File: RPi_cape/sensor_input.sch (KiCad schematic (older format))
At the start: 39 parts, among them U5 LM2903, U6 LMC7101B, U7 LMC7101B

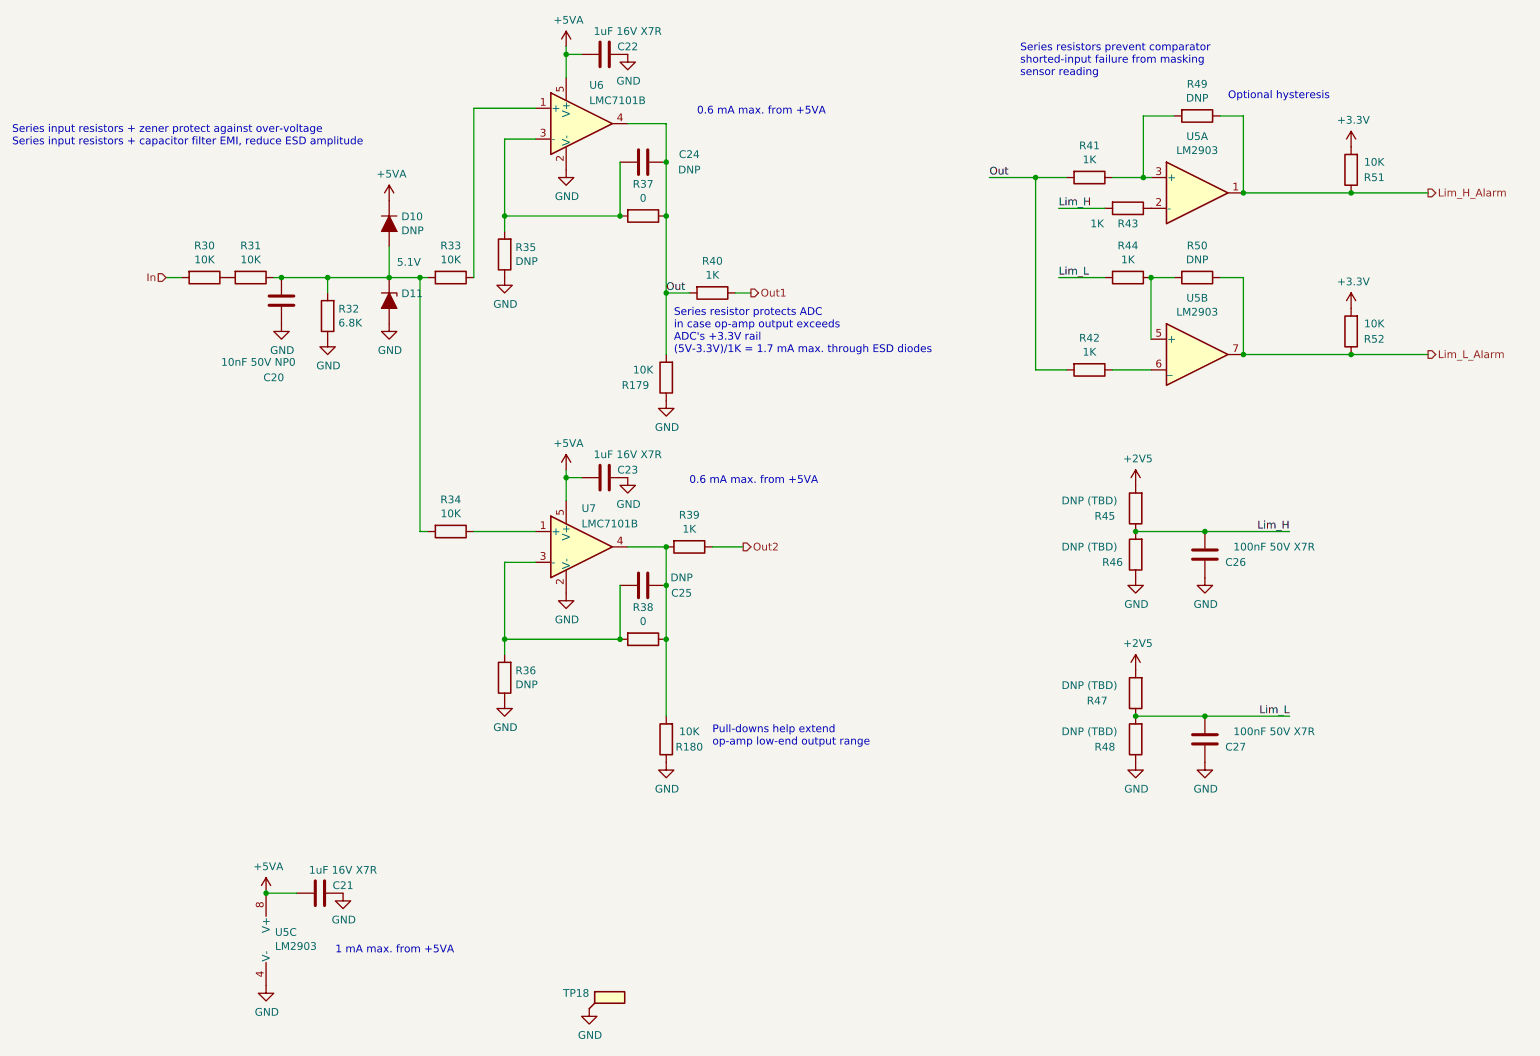
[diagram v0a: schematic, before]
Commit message: Analog upgrades and extra encoder connectors
Renamed a few files
Removed "costing BOM" as difficult to keep up to date, easy to regenerate
Toughened under-voltage detect circuits by adding hysteresis to +5V detect for +BATT diode-OR (R236), filtering to power-down alarm detect input (C85)
Added connector options (J15, J21) for Grayhill C14-series rotary encoder with cable
Changed R190 from 3K to 2.4K to increase overhead on base current required for saturation, and consolidate BOM
Added 3 solderable testpoints for expanding CPLD pin options (TP44-46), adjusted some CPLD pin assignments to allow physical routing to pins
Fixed valve motion detector by changing comparator's hysteresis to AC-only, changing NPN's series resistor to 1K (allows low-enough DC level to count as logic low), and adding optional filtering cap C115 to offset divider
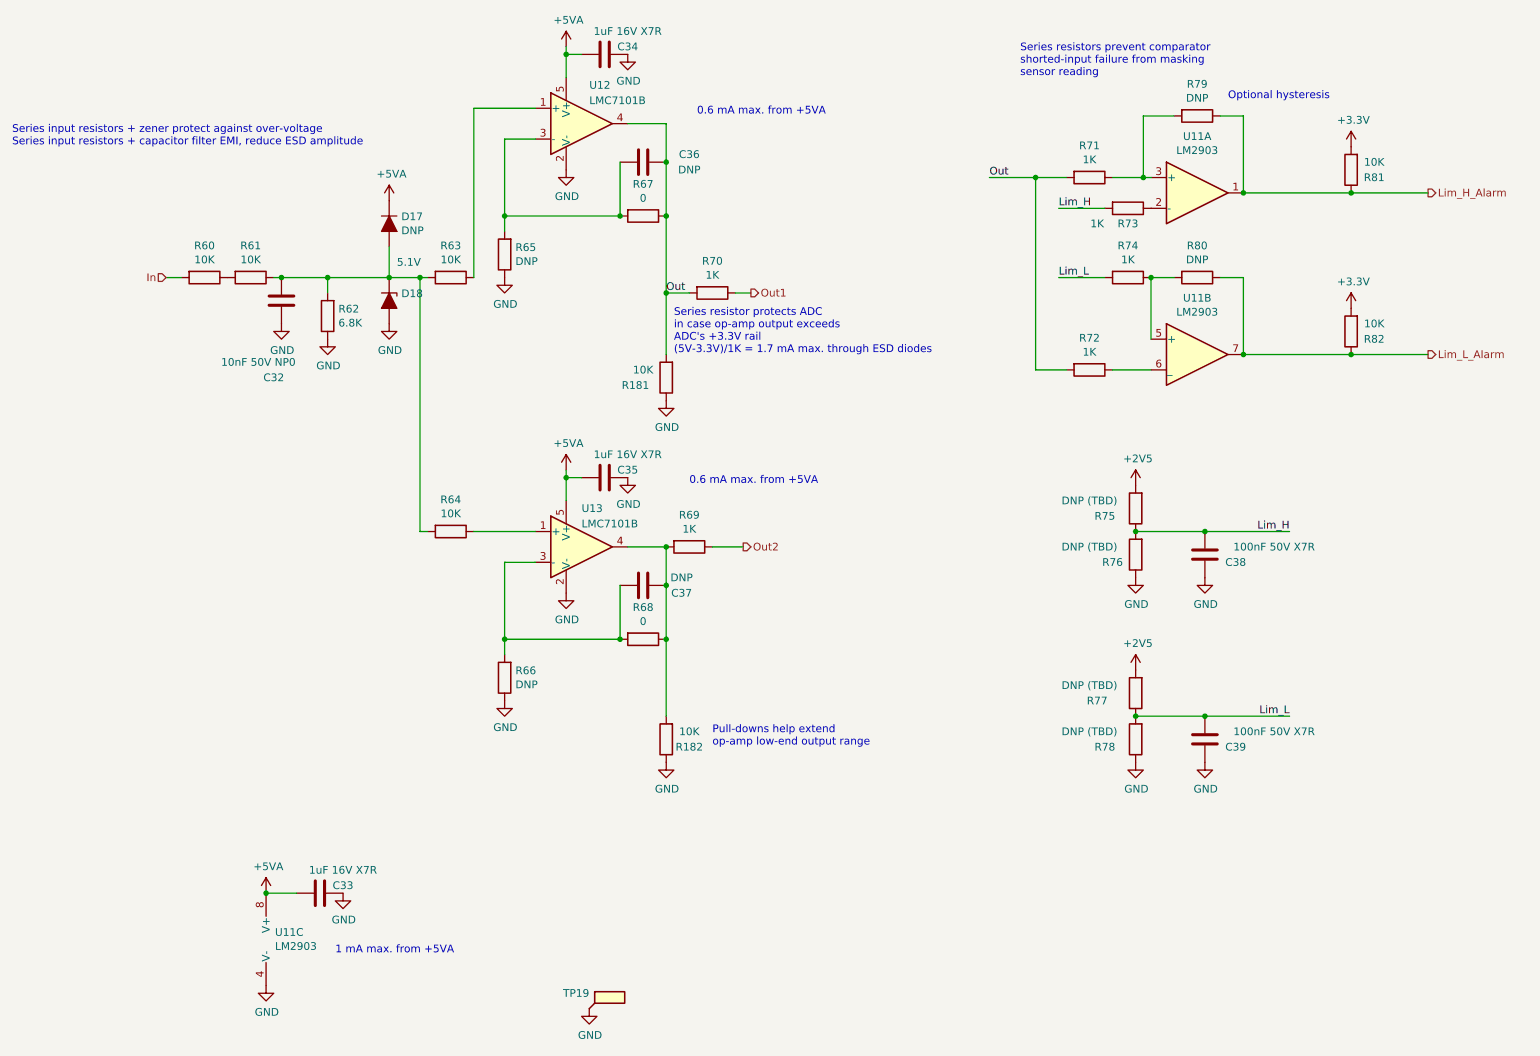
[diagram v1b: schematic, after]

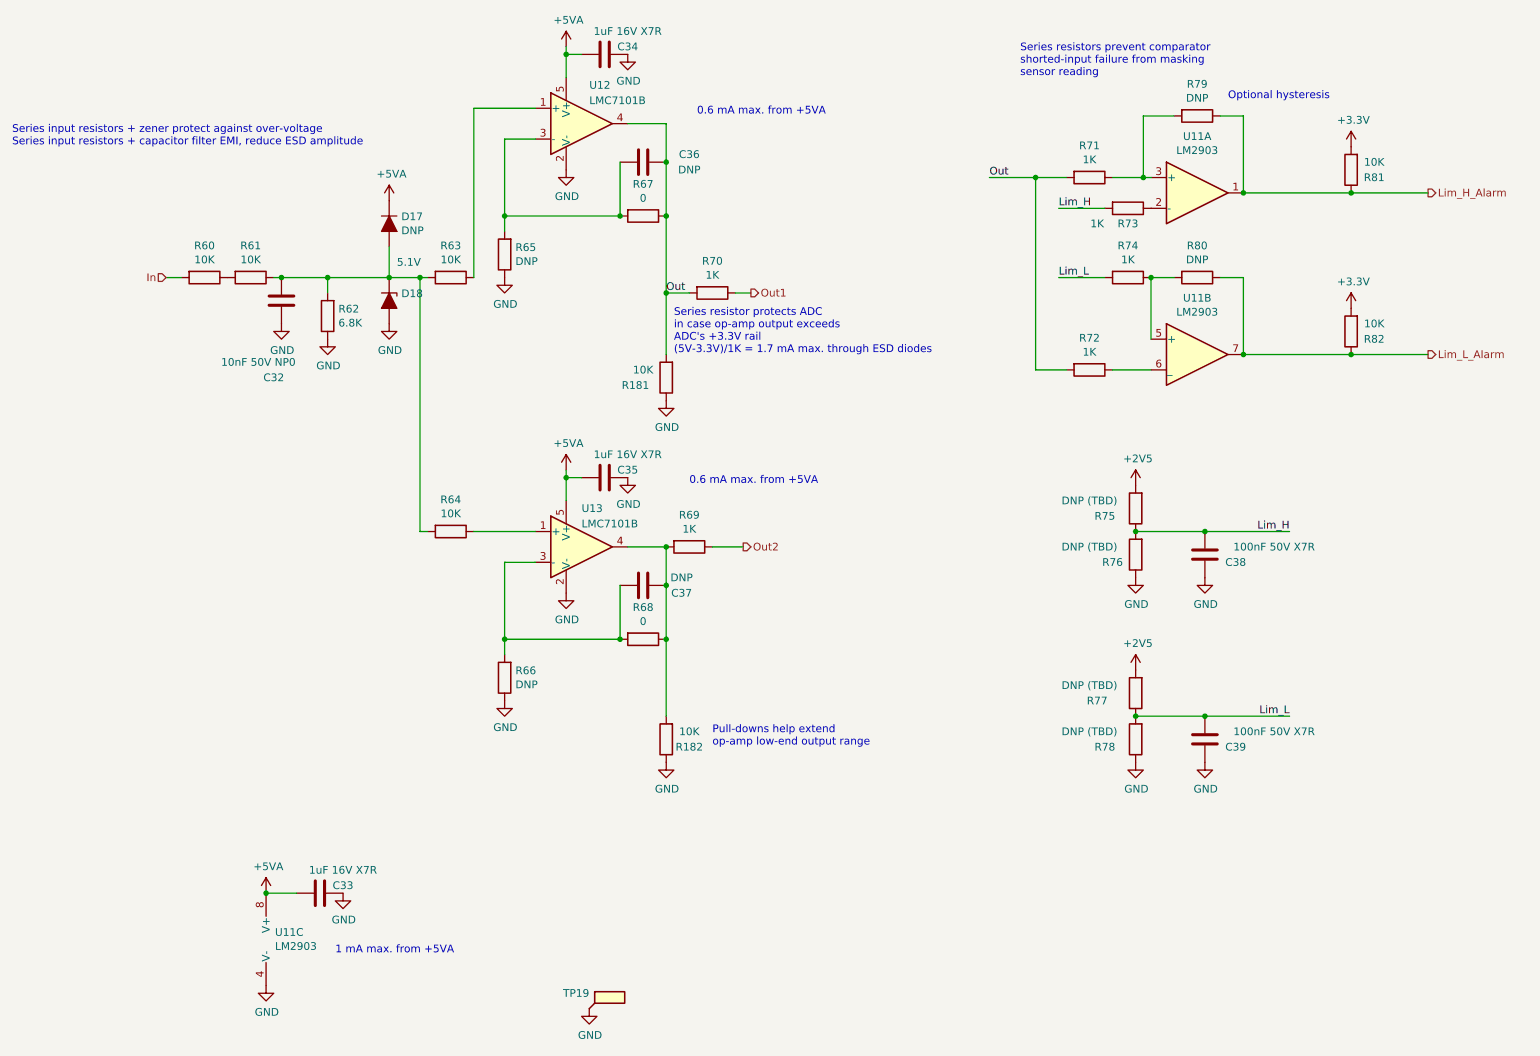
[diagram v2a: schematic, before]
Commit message: Admin (naming, license), improvements based on testing
Updated name on schematic, PCB silkscreen
Added 3 mounting holes on inside area of board for better mechanical robustness
Removed extra unused pressure sensor barb packages from library
Fixed Phoenix spring connector footprints, and added 3D models from Phoenix website
Added 3D models to TE encoder connector footprints, QFP-100 for CPLD, and 5019 testpoint
Changed DIAG_EN pin connection from valve drivers from +24V (too high) to +3.3V
Added CERN licensing terms
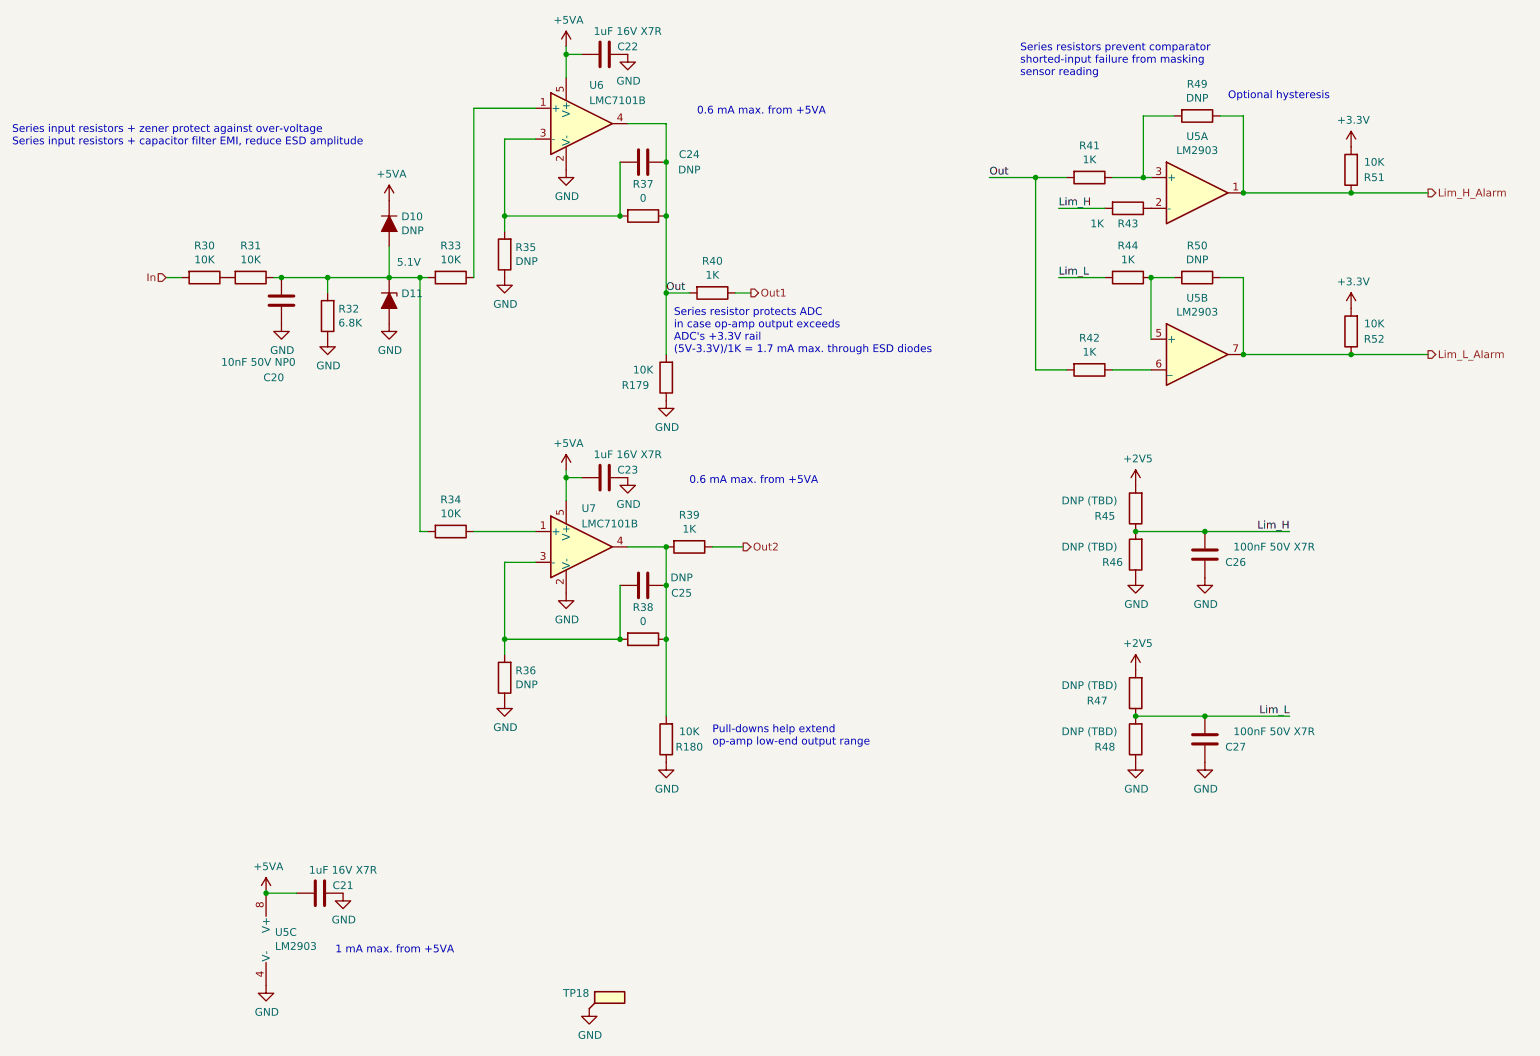
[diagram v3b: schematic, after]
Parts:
- TP18: footprint TestPoint:TestPoint_Keystone_5019_Minature -> Ventilator:TestPoint_Keystone_5019_Minature

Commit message: Design update based on changed software/firmware/pneumatics reqs
Swapped Max V CPLD for Max 10 FPGA
Removed +1.8V regulator and monitoring (in power-down alarm) because Max 10 FPGA has internal regulator
Changed FPGA's valve-enable pull-downs from 1K to 10K because Max 10 floats the outputs during power-up/programming (instead of Max V's internal pull-ups)
Changed low-pressure sensor from BMP388 to MS5607 for more manufacturable footprint / high availability, and moved all digital pressure sensors to daughterboard for repairability
Changed single op-amps in analog pressure sensor inputs / valve motion detect circuits to TLV6001 for better bias current, correct footprint
Removed excessive DNP components in analog pressure sensor inputs to ease routing with new op-amps
Added double-inverted hysteresis circuit to valve motion detect that won't drive U38's '+' input above the rail and cause latchup
Added optional pull-down resistors to valve-motiion-detect op-amps to allow output voltages to swing to zero
Added optional filter caps to ADC sensor inputs
Added pull-down to O2 sensor input for testing with sensor unplugged
Increased ADC input resistors (in analog sensor inputs) from 1K to 3.3K to avoid "lifting" +3.3V rail voltage in case of fault
Increased hole sizes to 3.7 mm for fitting #6 screws, to match some threaded vibration-damping bumpers from Joost
Fixed F.Fab-layer component reference text in custom footprints
Updated manufacturing files
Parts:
- removed R35, R36: DNP, Resistor_SMD:R_1206_3216Metric, symbol Device:R
- removed R37, R38: 0, Resistor_SMD:R_1206_3216Metric, symbol Device:R
- C24, C25: footprint Capacitor_SMD:C_0805_2012Metric -> Capacitor_SMD:C_0603_1608Metric; DNI (none) -> DNI
- D10, R45, R46, R47, R48, R49, R50: DNI (none) -> DNI
- R39, R40: value 1K -> 3.3K; Part Number RK73H2BTTD1001F -> RK73H2BTTD3301F
- U6, U7: value LMC7101B -> TLV6001; symbol Amplifier_Operational:LMV321 -> Amplifier_Operational:MCP601-xOT; Part Number LMC7101BIM5/NOPB -> TLV6001IDBVR
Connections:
- net GND: now also C24.1, C25.1
- net Out: now also U6.1; no longer C24.1
- net Out1: now also C25.2
- net Out2: now also C24.2
- net at R34.1: now also U7.3 (+); no longer U7.1 (+)
- net at R180.2, R39.2, U7.4 (-): now also U7.1; no longer C25.1
- net at R33.1: now also U6.3 (+); no longer U6.1 (+)
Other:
- note added: "0.1 mA max. from +5VA"
- note added: "Series resistor protects ADC\nin case op-amp output exceeds\nADC's +3.3V rail\n(5V-3.3V)/3.3K = 0.5 mA max. through ESD diodes\n\nIf all 3 sensor inputs are fully over-driven,\nthis will add ~~1.5 mA to +3.3V rail, which is\neasily sunk by power LED and misc. pull-ups"
- note removed: "0.6 mA max. from +5VA"
- note removed: "Series resistor protects ADC\nin case op-amp output exceeds\nADC's +3.3V rail\n(5V-3.3V)/1K = 1.7 mA max. through ESD diodes"
